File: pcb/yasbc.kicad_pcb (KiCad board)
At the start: 4 copper layers, 100 x 100 mm, 173 parts, among them J1 BOOT, J10 Conn_02x20_Odd_Even, J2 USB TTY, J3 AudioJack3, J4 1V5, J5 3V3, J6 1V2, J7 USB DEV, J8 Micro_SD_Card, J9 USB HOST, Q1 AO3401A, Q2 AO3401A, SW1 RESET, SW2 SW_SPDT, SW3 SW_SPDT, SW4 SW_SPDT, SW5 SW_SPDT, SW6 SW_5WAY, U1 BCT2028, U3 Allwinner_A13, U4 CH340E, U5 TD6810, U6 SE5120, U7 K4B4G1646E, U8 MPU-6050, Y1 24M

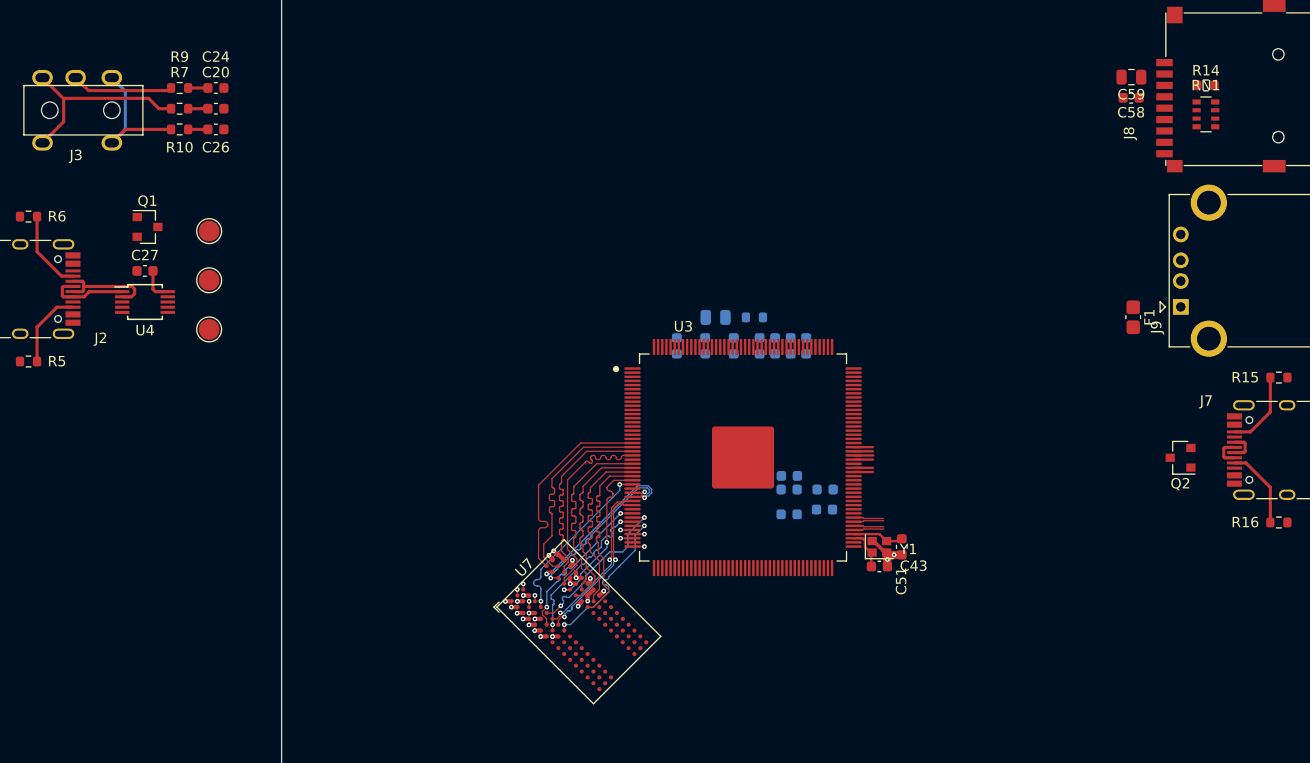
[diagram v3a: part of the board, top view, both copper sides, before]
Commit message: Routed DDR3 clock, address, command and control signals
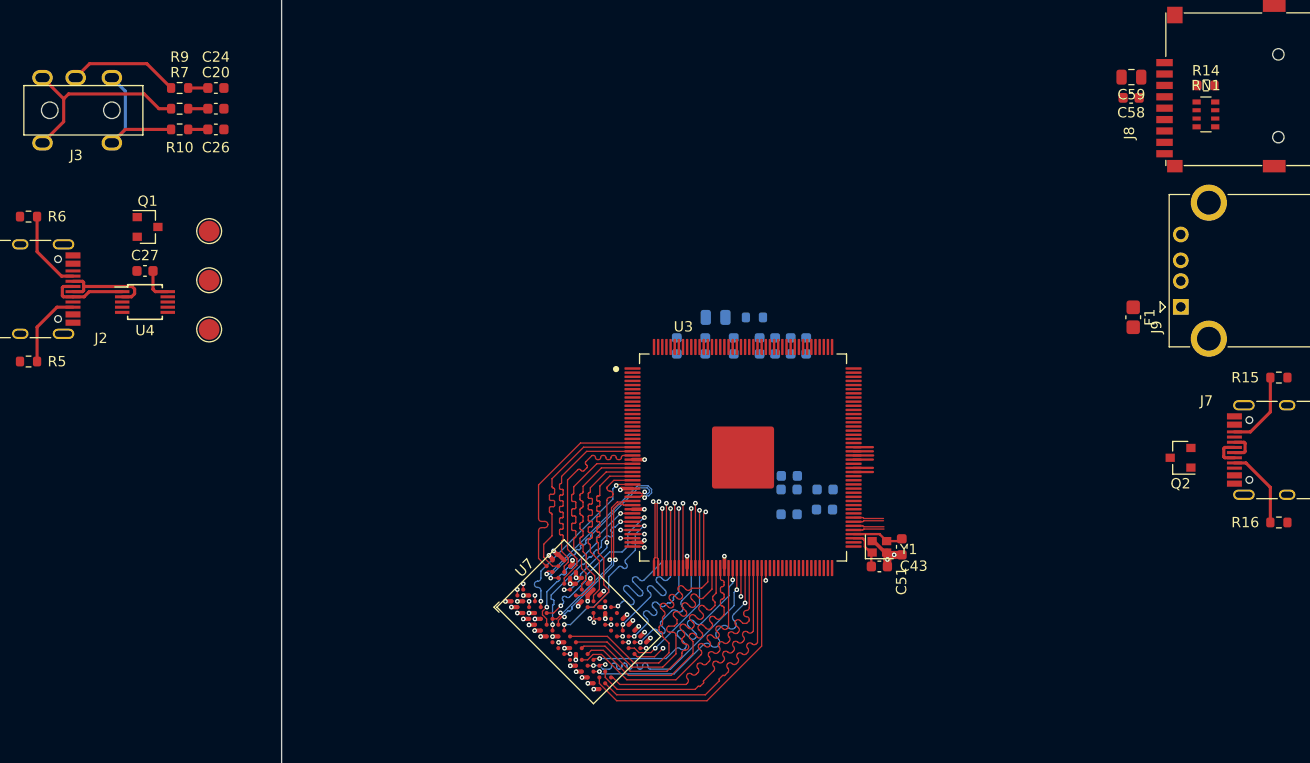
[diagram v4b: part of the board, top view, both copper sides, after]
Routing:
- net /DDR3_A7: track 0.00 -> 26.7 mm
- net /DDR3_RST: track 0.00 -> 26.5 mm
- net /DDR3_CAS: track 0.00 -> 26.5 mm
- net /DDR3_BA0: track 0.00 -> 26.5 mm
- net /DDR3_RAS: track 0.00 -> 26.5 mm
- net /DDR3_BA2: track 0.00 -> 26.5 mm
- net /DDR3_WE: track 0.00 -> 26.5 mm
- net /DDR3_A9: track 0.00 -> 26.5 mm
- net /DDR3_A13: track 0.00 -> 26.4 mm
- net /DDR3_ODT: track 0.00 -> 23.6 mm, vias 0 -> 2
- net /DDR3_A14: track 0.00 -> 23.6 mm, vias 0 -> 2
- net /DDR3_A11: track 0.00 -> 23.6 mm, vias 0 -> 2
- net /DDR3_A1: track 0.00 -> 23.6 mm, vias 0 -> 2
- net /DDR3_A8: track 0.00 -> 23.6 mm, vias 0 -> 2
- net /DDR3_A12: track 0.00 -> 23.6 mm, vias 0 -> 2
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
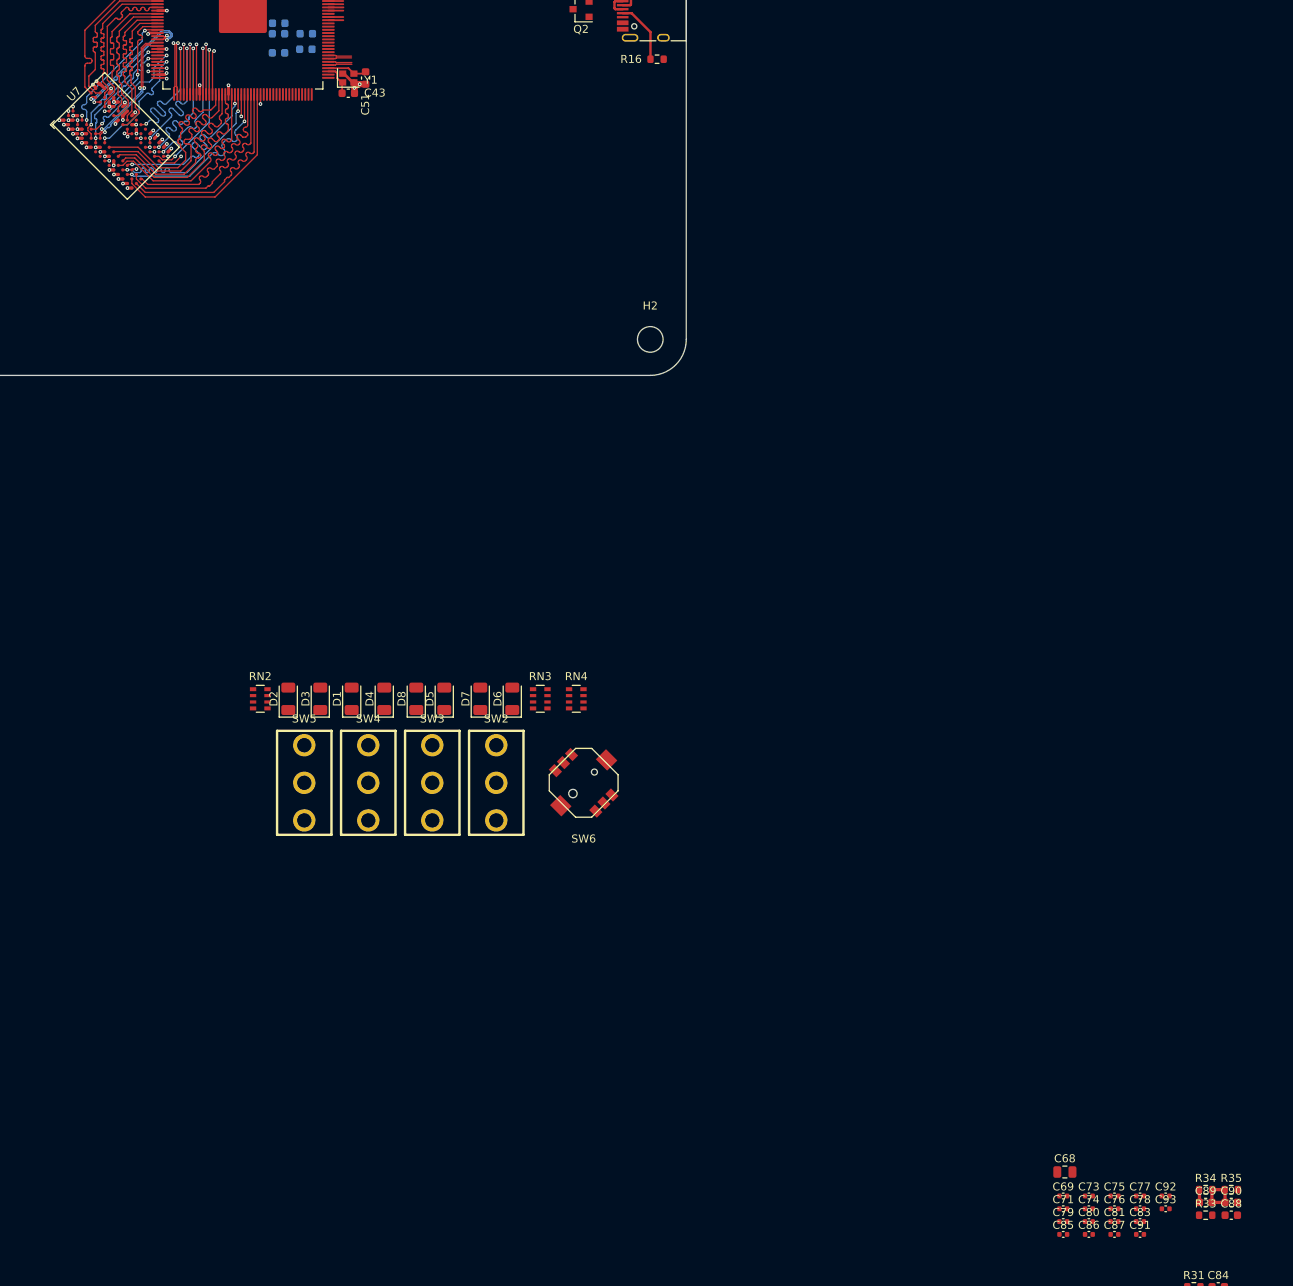
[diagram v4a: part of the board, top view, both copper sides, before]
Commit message: Worked on DDR3 decoupling caps
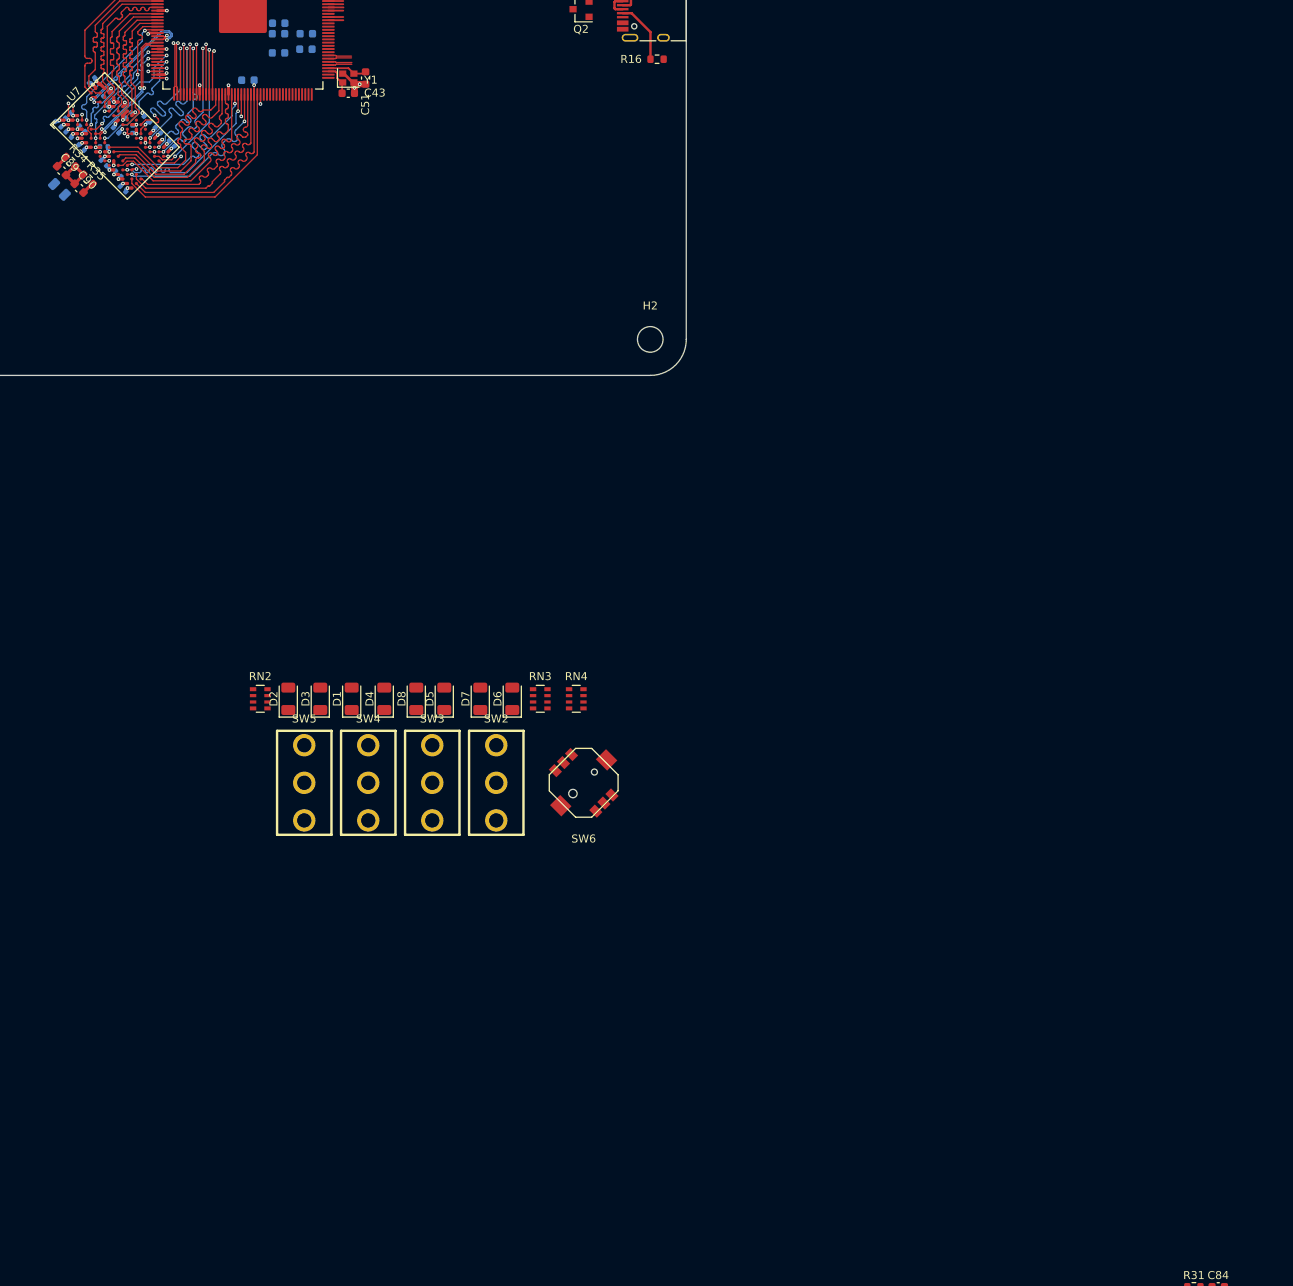
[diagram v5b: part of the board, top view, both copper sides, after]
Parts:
- removed C83: 0.1u, Capacitor_SMD:C_0402_1005Metric
- C68, C69, C71, C73, C74, C75, C76, C77, C78, C79, C80, C81, C85, C86, C87, C88, C91, C92, C93: moved to B.Cu
- R33: footprint Resistor_SMD:R_0603_1608Metric -> Resistor_SMD:R_0402_1005Metric; moved to B.Cu
- moved C89 192.6 mm to (58.9, -35.6), turned to -45 degrees
- moved C90 191.9 mm to (61.1, -33.4), turned to -45 degrees
- moved R34 191.4 mm to (60.0, -36.7), turned to -45 degrees
- moved R35 190.7 mm to (62.2, -34.5), turned to -45 degrees
- moved R33 190.5 mm to (69.6, -42.0), turned to 135 degrees
- moved C77 190.4 mm to (58.5, -41.4), turned to -45 degrees
- moved C81 190.3 mm to (59.8, -42.5), turned to 45 degrees
- moved C78 189.6 mm to (59.8, -40.1), turned to -45 degrees
- moved C93 188.1 mm to (65.7, -40.6), turned to -45 degrees
- moved C88 187.7 mm to (82.2, -46.9), turned to 180 degrees
- moved C76 186.5 mm to (65.1, -43.9), turned to -135 degrees
- moved C85 186.1 mm to (64.5, -45.2), turned to -135 degrees
- moved C71 186.1 mm to (62.7, -46.9), turned to 45 degrees
- moved C91 184.7 mm to (71.0, -40.6), turned to 135 degrees
- moved C87 184.1 mm to (64.2, -36.5), turned to -45 degrees
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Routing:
- net GND: track 34.8 -> 44.6 mm, vias 21 -> 23
- net +1V5: track 18.0 -> 27.7 mm
- net Net-(C89-Pad2): track 6.44 -> 13.4 mm, vias 0 -> 2
- net Net-(R33-Pad1): track 0.00 -> 2.07 mm, vias 0 -> 1
- net /DDR3_RST: track 26.5 -> 28.3 mm, vias 0 -> 1
- added copper zone on In1.Cu, net GND

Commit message: WIP
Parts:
- moved C86 2.66 mm to (65.7, -40.8), turned to -45 degrees
- moved C93 2.61 mm to (63.7, -38.9), turned to 0 degrees
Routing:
- net Net-(C89-Pad2): track 13.4 -> 16.5 mm
- net +1V5: track 27.7 -> 25.6 mm, vias 22 -> 24
- net GND: track 44.6 -> 44.1 mm, vias 23 -> 25
- added copper zone on In2.Cu, net +1V5

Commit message: PMIC PCB layout
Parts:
- removed J2: USB TTY, Connector_USB:USB_C_Receptacle_HRO_TYPE-C-31-M-12
- removed RN3: 1K, Resistor_SMD:R_Array_Convex_4x0603
- removed RN4: 47K, Resistor_SMD:R_Array_Convex_4x0603
- removed U8: MPU-6050, Sensor_Motion:InvenSense_QFN-24_4x4mm_P0.5mm
- added C100: 100n, Capacitor_SMD:C_0603_1608Metric, F.Cu at (262.1, -104.6)
- added C101: 100n, Capacitor_SMD:C_0603_1608Metric, F.Cu at (237.9, -64.2)
- added C102: 22p, Capacitor_SMD:C_0603_1608Metric, F.Cu at (229.9, -59.5)
- added C103: 100n, Capacitor_SMD:C_0603_1608Metric, F.Cu at (217.2, -57.1)
- added C104: 100n, Capacitor_SMD:C_0603_1608Metric, F.Cu at (274.1, -102.1)
- added C105: 22p, Capacitor_SMD:C_0603_1608Metric, F.Cu at (226.3, -69.5)
- added C106: 100n, Capacitor_SMD:C_0603_1608Metric, F.Cu at (244.4, -89.1)
- added C107: 100n, Capacitor_SMD:C_0603_1608Metric, F.Cu at (225.9, -57.0)
- added C45: 100n, Capacitor_SMD:C_0603_1608Metric, F.Cu at (217.9, -64.6)
- added C53: 100n, Capacitor_SMD:C_0603_1608Metric, F.Cu at (233.9, -62.0)
- added C6: 100n, Capacitor_SMD:C_0603_1608Metric, F.Cu at (84.1, -98.3)
- added C83: 100n, Capacitor_SMD:C_0603_1608Metric, F.Cu at (234.3, -72.0)
- added C94: 100n, Capacitor_SMD:C_0603_1608Metric, F.Cu at (257.7, -94.6)
- added C95: 100n, Capacitor_SMD:C_0603_1608Metric, F.Cu at (237.9, -66.7)
- added C96: 100n, Capacitor_SMD:C_0603_1608Metric, F.Cu at (217.0, -47.0)
- added C97: 100n, Capacitor_SMD:C_0603_1608Metric, F.Cu at (261.7, -97.1)
- added C98: 100n, Capacitor_SMD:C_0603_1608Metric, F.Cu at (209.0, -49.2)
- added C99: 100n, Capacitor_SMD:C_0603_1608Metric, F.Cu at (254.2, -85.1)
- added J11: Conn_02x20_Odd_Even, Connector_PinHeader_2.54mm:PinHeader_2x20_P2.54mm_Vertical, F.Cu at (168.9, -103.6)
- added L2: 2.2u, yasbc:Inductor_5.2x5.8x4.5mm, F.Cu at (93.9, -92.9)
- added R36: 5.1K, Resistor_SMD:R_0603_1608Metric, F.Cu at (213.4, -67.1)
- added R37: 5.1K, Resistor_SMD:R_0603_1608Metric, F.Cu at (218.3, -71.5)
- added R38: 10K, Resistor_SMD:R_0603_1608Metric, F.Cu at (193.0, -47.2)
- added R39: 100, Resistor_SMD:R_0603_1608Metric, F.Cu at (242.2, -76.9)
- added R40: 100, Resistor_SMD:R_0603_1608Metric, F.Cu at (274.1, -104.6)
- added R41: 22, Resistor_SMD:R_0603_1608Metric, F.Cu at (240.4, -89.4)
- added R42: 2K, Resistor_SMD:R_0603_1608Metric, F.Cu at (254.2, -80.1)
- added R43: 2K, Resistor_SMD:R_0603_1608Metric, F.Cu at (190.0, -74.6)
- added R44: 22, Resistor_SMD:R_0603_1608Metric, F.Cu at (209.8, -59.6)
- added R45: 10K, Resistor_SMD:R_0603_1608Metric, F.Cu at (222.3, -72.9)
- added R46: 22, Resistor_SMD:R_0603_1608Metric, F.Cu at (205.2, -54.2)
- added R47: 10K, Resistor_SMD:R_0603_1608Metric, F.Cu at (209.8, -62.1)
- added R48: 5.1K, Resistor_SMD:R_0603_1608Metric, F.Cu at (225.4, -76.7)
- added R49: 5.1K, Resistor_SMD:R_0603_1608Metric, F.Cu at (226.1, -80.0)
- added R50: 240 1%, Resistor_SMD:R_0603_1608Metric, F.Cu at (194.0, -74.6)
- added R51: 5.1K, Resistor_SMD:R_0603_1608Metric, F.Cu at (253.6, -95.2)
- added R52: 5.1K, Resistor_SMD:R_0603_1608Metric, F.Cu at (246.2, -83.6)
- C1, C25: value 1u -> 100n
- C10, C12: value 0.1u -> 6.8p; moved to F.Cu
- C11, C13: value 0.1u -> 33p; moved to F.Cu
- C14, C8: value 10u -> 100n; moved to F.Cu
- C15, C16, C17, C21, C3, C33, C37, C38, C4, C41, C42, C46, C47, C49, C50, C60, C7, C88, C9: value 0.1u -> 100n; moved to F.Cu
- C18, C19, C20, C24, C26, C27, C39, C58, C70, C72, C82, C90: value 0.1u -> 100n
- C2, C54, C55, C68: value 47u -> 100n; footprint Capacitor_SMD:C_0805_2012Metric -> Capacitor_SMD:C_0603_1608Metric; moved to F.Cu
- C22, C23, C28, C34, C36: value 0.1u -> 10u; moved to F.Cu
- C30, C35, C57: moved to F.Cu
- C31, C62, C89: value 0.1u -> 10u
- C32: value DNF -> 10u
- C40: value 10u -> 47u; moved to F.Cu
- C43, C51: value 22p -> 100n
- C48, C63, C64, C65, C66, C67: value 10u -> 100n
- C5: value DNF -> 100n
- C52: value 1u -> 100n; moved to F.Cu
- C56: value 0.1u -> 47u; moved to F.Cu
- C59: value 47u -> 100n; footprint Capacitor_SMD:C_0805_2012Metric -> Capacitor_SMD:C_0603_1608Metric
- C61: value 0.1u -> 1u; moved to F.Cu
- C69: value 0.1u -> 10u; footprint Capacitor_SMD:C_0402_1005Metric -> Capacitor_SMD:C_0603_1608Metric; moved to F.Cu
- C71, C75, C76, C77, C78, C79, C80, C81, C85, C86, C91, C92, C93: value 0.1u -> 100n; footprint Capacitor_SMD:C_0402_1005Metric -> Capacitor_SMD:C_0603_1608Metric; moved to F.Cu
- C73, C74, C87: value 0.1u -> 47u; footprint Capacitor_SMD:C_0402_1005Metric -> Capacitor_SMD:C_0603_1608Metric; moved to F.Cu
- C84: value 0.1u 50V -> 100n 50V
- D1: value LED_Small -> 5V; footprint LED_SMD:LED_1206_3216Metric -> Diode_SMD:D_SMB
- D9: value 5V -> LED_Small; footprint Diode_SMD:D_SMB -> LED_SMD:LED_1206_3216Metric
- F1: footprint Fuse:Fuse_0805_2012Metric_Castellated -> Fuse:Fuse_0805_2012Metric_Pad1.15x1.40mm_HandSolder
- J1: value BOOT -> USB TTY; footprint Connector_PinHeader_2.54mm:PinHeader_1x02_P2.54mm_Vertical -> Connector_USB:USB_C_Receptacle_HRO_TYPE-C-31-M-12
- J10: value Conn_02x20_Odd_Even -> AudioJack3; footprint Connector_PinHeader_2.54mm:PinHeader_2x20_P2.54mm_Vertical -> yasbc:AudioJack
- J3: value AudioJack3 -> USB DEV; footprint yasbc:AudioJack -> Connector_USB:USB_C_Receptacle_HRO_TYPE-C-31-M-12
- J5: value 3V3 -> 1V5
- J6: value 1V2 -> USB HOST; footprint Connector_PinHeader_2.54mm:PinHeader_1x02_P2.54mm_Vertical -> Connector_USB:USB_A_CONNFLY_DS1095-WNR0
- J7: value USB DEV -> 1V5; footprint Connector_USB:USB_C_Receptacle_HRO_TYPE-C-31-M-12 -> Connector_PinHeader_2.54mm:PinHeader_1x02_P2.54mm_Vertical
- J8: value Micro_SD_Card -> 1V5; footprint yasbc:microSD -> Connector_PinHeader_2.54mm:PinHeader_1x02_P2.54mm_Vertical
- J9: value USB HOST -> BOOT; footprint Connector_USB:USB_A_CONNFLY_DS1095-WNR0 -> Connector_PinHeader_2.54mm:PinHeader_1x02_P2.54mm_Vertical
- L1: value 4.7u -> 2.2u; footprint Inductor_SMD:L_1008_2520Metric -> yasbc:Inductor_5.2x5.8x4.5mm
- R1, R12, R2, R20, R21, R22: value 10K -> 5.1K
- R10: value 22 -> 402K
- R11: value 10K -> 200K; moved to F.Cu
- R13: value 200K -> 5.1K; moved to F.Cu
- R15, R24, R25, R26, R31, R32: value 5.1K -> 47K
- R16: value 5.1K -> 10K
- R17: value 240 1% -> 10K; moved to F.Cu
- R18, R19: value 2K -> 10K; moved to F.Cu
- R27: value 10K -> 2K
- R28: value 100 -> 2K
- R29: value 100 -> 240 1%
- R3: value 5.1K -> 887
- R33: value 240 1% -> 47K; footprint Resistor_SMD:R_0402_1005Metric -> Resistor_SMD:R_0603_1608Metric; moved to F.Cu
- R34: value 2K -> 200K
- R35: value 2K -> 47K
- R4: value 5.1K -> 280K
- R5: value 5.1K -> 200K
- R6: value 5.1K -> 562K
- R7: value 22 -> 100K
- R8: value 10K -> 604K
- R9: value 22 -> 232K
- RN1: value 47K -> 1K
- SW1: value RESET -> SW_SPDT; footprint yasbc:HYP-1TS002B-2500-4300-CT -> yasbc:SS-12D10
- SW5: value SW_SPDT -> SW_5WAY; footprint yasbc:SS-12D10 -> yasbc:Switches_ALPS-SKRHAAE010
- SW6: value SW_5WAY -> RESET; footprint yasbc:Switches_ALPS-SKRHAAE010 -> yasbc:HYP-1TS002B-2500-4300-CT
- U1: value BCT2028 -> LM26480; footprint Package_TO_SOT_SMD:SOT-23-5 -> Package_DFN_QFN:WQFN-24-1EP_4x4mm_P0.5mm_EP2.6x2.6mm
- U3: value Allwinner_A13 -> CH340E; footprint yasbc:LQFP-176_20x20mm_P0.4mm_PAD -> Package_SO:MSOP-10_3x3mm_P0.5mm
- U4: value CH340E -> Allwinner_A13; footprint Package_SO:MSOP-10_3x3mm_P0.5mm -> yasbc:LQFP-176_20x20mm_P0.4mm_PAD
- U5: value TD6810 -> uSD_Card; footprint Package_TO_SOT_SMD:TSOT-23-5 -> yasbc:microSD
- U6: value SE5120 -> MPU-6050; footprint Package_TO_SOT_SMD:SOT-223-3_TabPin2 -> Sensor_Motion:InvenSense_QFN-24_4x4mm_P0.5mm
- moved C61 331.1 mm to (258.2, -87.1), turned to 0 degrees
- moved C60 330.1 mm to (257.7, -97.1), turned to 0 degrees
- moved C15 326.2 mm to (261.7, -99.6)
- moved J6 323.6 mm to (57.4, -96.4), turned to 180 degrees
- moved C29 317.8 mm to (82.1, -100.1)
- moved C54 316.9 mm to (265.7, -94.6), turned to 0 degrees
- moved C37 310.7 mm to (248.4, -88.6)
- moved C41 309.4 mm to (246.3, -73.5)
- moved L1 308.8 mm to (79.5, -92.9), turned to -90 degrees
- moved C35 307.9 mm to (250.3, -76.0), turned to 0 degrees
- moved C33 305.5 mm to (242.2, -79.4)
- moved R18 303.2 mm to (226.3, -72.0), turned to 0 degrees
- moved R13 301.4 mm to (242.3, -71.8), turned to 0 degrees
- moved C5 300.6 mm to (89.1, -98.2)
- moved C1 296.7 mm to (83.1, -95.9), turned to 90 degrees
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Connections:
- C1 pad 1: VBUS -> GND
- C1 pad 2: GND -> +5V
- C10 pad 1: +3V3 -> +1V2
- C10 pad 2: GND -> /P_FB1
- C11 pad 1: +1V2 -> /P_FB1
- C12 pad 2: GND -> /P_FB2
- C13 pad 1: +1V2 -> /P_FB2
- C14 pad 1: +3V3 -> +1V8
- C15 pad 1: +3V3 -> +1V8
- C16 pad 1: +1V2 -> +1V8
- C17 pad 1: +3V3 -> +1V8
- C18 pad 1: /RESET -> +1V2
- C19 pad 1: Net-(C19-Pad1) -> +3V3
- C2 pad 1: +1V2 -> +5V
- C20 pad 1: Net-(C20-Pad1) -> +1V8
- C21 pad 1: +3V3 -> +1V8
- C24 pad 1: Net-(C24-Pad1) -> +1V8
- C25 pad 1: Net-(C25-Pad1) -> +3V3
- C26 pad 1: Net-(C26-Pad1) -> +1V8
- C27 pad 1: +3V3 -> +1V5
- C28 pad 1: Net-(C28-Pad1) -> +1V8
- C29 pad 1: VBUS -> +1V5
- C3 pad 1: +1V2 -> +5V
- C30 pad 1: Net-(C28-Pad1) -> /SW_DOWN
- C31 pad 1: VBUS -> /SW_UP
- C32 pad 1: Net-(C32-Pad1) -> /SW_RIGHT
- C33 pad 1: +1V5 -> /SW_R2R
- C34 pad 1: +1V2 -> /SW_CENTER
- C35 pad 1: GND -> /SW_LEFT
- C35 pad 2: +3V3 -> GND
- C36 pad 1: Net-(C36-Pad1) -> +3V3
- C37 pad 1: +1V5 -> +1V2
- C38 pad 1: +1V2 -> +3V3
- C39 pad 1: Net-(C39-Pad1) -> +1V2
- C4 pad 1: +1V2 -> +5V
- C40 pad 1: Net-(C36-Pad1) -> +1V2
- C41 pad 1: +1V5 -> +3V3
- C43 pad 1: Net-(C43-Pad1) -> +1V2
- C44 pad 1: Net-(C44-Pad1) -> +3V3
- C46 pad 1: +1V5 -> +1V2
- C48 pad 1: Net-(C39-Pad1) -> +3V3
- C49 pad 1: +1V5 -> +3V3
- C5 pad 1: Net-(C5-Pad1) -> +3V3
- C51 pad 1: Net-(C51-Pad1) -> +1V2
- C52 pad 1: Net-(C52-Pad1) -> +3V3
- C54 pad 1: +1V5 -> /A13_SVREF
- C55 pad 1: +1V2 -> +3V3
- C56 pad 1: Net-(C56-Pad1) -> +3V3
- C57 pad 1: Net-(C56-Pad1) -> +3V3
- C58 pad 1: +3V3 -> Net-(C58-Pad1)
- C59 pad 1: +3V3 -> +1V5
- C60 pad 1: +1V5 -> +1V2
- C60 pad 2: Net-(C60-Pad2) -> GND
- C61 pad 1: Net-(C60-Pad2) -> Net-(C61-Pad1)
- C62 pad 1: /SW_R2R -> Net-(C58-Pad1)
- C63 pad 1: /SW_DOWN -> +1V5
- C64 pad 1: /SW_UP -> +1V2
- C65 pad 1: /SW_RIGHT -> +1V5
- C66 pad 1: /SW_CENTER -> +1V2
- C67 pad 1: /SW_LEFT -> +1V5
- C68 pad 1: +1V5 -> +1V2
- C69 pad 1: +1V5 -> Net-(C69-Pad1)
- C7 pad 1: +1V2 -> GND
- C7 pad 2: GND -> +3V3
- C70 pad 1: +3V3 -> Net-(C69-Pad1)
- C72 pad 1: +3V3 -> +1V2
- C74 pad 1: +1V5 -> +1V2
- C75 pad 1: +1V5 -> Net-(C75-Pad1)
- C76 pad 1: +1V5 -> /RESET
- C77 pad 1: +1V5 -> /DDR3_RST
- C78 pad 1: +1V5 -> Net-(C78-Pad1)
- C79 pad 2: GND -> /DDR3_REF
- C8 pad 1: +3V3 -> +1V8
- C80 pad 1: +1V5 -> /DDR3_REF
- C81 pad 1: +1V5 -> Net-(C81-Pad1)
- C85 pad 1: +1V5 -> Net-(C85-Pad1)
- C86 pad 1: +1V5 -> +3V3
- C88 pad 1: /DDR3_RST -> +1V5
- C89 pad 1: +1V5 -> Net-(C85-Pad1)
- C89 pad 2: Net-(C89-Pad2) -> GND
- C9 pad 1: +1V2 -> +1V8
- C90 pad 1: Net-(C89-Pad2) -> +1V5
- D1 pad 1: GND -> +5V
- D1 pad 2: Net-(D1-Pad2) -> GND
- D9 pad 1: VBUS -> GND
- D9 pad 2: GND -> Net-(D9-Pad2)
- F1 pad 2: VBUS -> +5V
- J4 pad 1: +1V5 -> +1V2
- J4 pad 2: Net-(C25-Pad1) -> GND
- J5 pad 2: Net-(C39-Pad1) -> GND
- J6 pad 1: +1V2 -> Net-(F1-Pad1)
- J6 pad 2: Net-(C44-Pad1) -> /USB_HOST_D-
- J8 pad 1: /SD_D2 -> +1V5
- J8 pad 2: /SD_D3 -> GND
- J9 pad 1: Net-(F1-Pad1) -> GND
- J9 pad 2: /USB_HOST_D- -> /BOOT
- L1 pad 1: Net-(L1-Pad1) -> /P_SW1
- L1 pad 2: Net-(C44-Pad1) -> +1V2
- Q1 pad 2: VBUS -> +5V
- Q1 pad 3: Net-(J2-PadA4) -> Net-(J1-PadA4)
- Q2 pad 2: VBUS -> +5V
- Q2 pad 3: Net-(J7-PadA4) -> Net-(J3-PadA4)
- R1 pad 1: Net-(C5-Pad1) -> Net-(J1-PadA5)
- R1 pad 2: VBUS -> GND
- R10 pad 1: Net-(C26-Pad1) -> +1V5
- R10 pad 2: Net-(J3-PadT) -> /P_FBL2
- R11 pad 1: +3V3 -> /P_FBL2
- R11 pad 2: Net-(R11-Pad2) -> GND
- R12 pad 1: Net-(C32-Pad1) -> Net-(J3-PadA5)
- R12 pad 2: VBUS -> GND
- R13 pad 1: Net-(C36-Pad1) -> Net-(J3-PadB5)
- R14 pad 1: +3V3 -> /SW_DOWN
- R14 pad 2: /SD_D1 -> GND
- R15 pad 1: Net-(J7-PadB5) -> /SW_UP
- R16 pad 1: Net-(J7-PadA5) -> /SW_R2R
- R16 pad 2: GND -> Net-(R16-Pad2)
- R17 pad 2: GND -> Net-(R17-Pad2)
- R18 pad 1: +1V5 -> Net-(R18-Pad1)
- R18 pad 2: Net-(C60-Pad2) -> Net-(R18-Pad2)
- R19 pad 1: Net-(C60-Pad2) -> Net-(R19-Pad1)
- R19 pad 2: GND -> Net-(R19-Pad2)
- R2 pad 1: +3V3 -> Net-(J1-PadB5)
- R2 pad 2: /BOOT -> GND
- R20 pad 1: /SW_R2R -> Net-(R17-Pad1)
- R20 pad 2: Net-(R20-Pad2) -> /SW_R2R
- R21 pad 1: Net-(R21-Pad1) -> Net-(R18-Pad1)
- R21 pad 2: Net-(R21-Pad2) -> Net-(R17-Pad1)
- R22 pad 1: Net-(R22-Pad1) -> Net-(R19-Pad1)
- R22 pad 2: Net-(R22-Pad2) -> Net-(R18-Pad1)
- R23 pad 1: Net-(R23-Pad1) -> GND
- R23 pad 2: Net-(R23-Pad2) -> Net-(R19-Pad1)
- R24 pad 1: Net-(R21-Pad1) -> /SW_RIGHT
- R24 pad 2: /SW_R2R -> GND
- R25 pad 1: Net-(R22-Pad1) -> /SW_CENTER
- R25 pad 2: Net-(R21-Pad1) -> GND
- R26 pad 1: Net-(R23-Pad1) -> /SW_LEFT
- R26 pad 2: Net-(R22-Pad1) -> GND
- R27 pad 1: GND -> +1V5
- R27 pad 2: Net-(R23-Pad1) -> /A13_SVREF
- R28 pad 1: Net-(R28-Pad1) -> /A13_SVREF
- R28 pad 2: /TTY_TX -> GND
- R29 pad 2: /TTY_RX -> GND
- R3 pad 1: +3V3 -> GND
- R3 pad 2: /I2C_SCL -> Net-(R3-Pad2)
- R30 pad 1: /SW_LEFT -> +3V3
- R30 pad 2: GND -> /SD_CMD
- R31 pad 2: /MPU_SCL -> /SD_D3
- R32 pad 2: /MPU_SDA -> /SD_D2
- R33 pad 1: Net-(R33-Pad1) -> +3V3
- R33 pad 2: GND -> /SD_D1
- R34 pad 1: +1V5 -> Net-(C58-Pad1)
- R34 pad 2: Net-(C89-Pad2) -> GND
- R35 pad 1: Net-(C89-Pad2) -> +3V3
- R35 pad 2: GND -> /SD_D0
- R4 pad 1: +3V3 -> +1V2
- R4 pad 2: /I2C_SDA -> /P_FB1
- R5 pad 1: Net-(J2-PadB5) -> /P_FB1
- R6 pad 1: Net-(J2-PadA5) -> +3V3
- R6 pad 2: GND -> /P_FB2
- R7 pad 1: Net-(C20-Pad1) -> /P_FB2
- R7 pad 2: Net-(J3-PadS) -> GND
- R8 pad 1: +3V3 -> +1V8
- R8 pad 2: /RESET -> /P_FBL1
- R9 pad 1: Net-(C24-Pad1) -> /P_FBL1
- R9 pad 2: Net-(J3-PadR) -> GND
- RN1 pad 1: /SD_D2 -> /LED3
- RN1 pad 2: /SD_D3 -> /LED1
- RN1 pad 3: /SD_CMD -> /LED2
- RN1 pad 4: /SD_D0 -> /LED4
- RN1 pad 5: +3V3 -> Net-(D5-Pad2)
- RN1 pad 6: +3V3 -> Net-(D4-Pad2)
- RN1 pad 7: +3V3 -> Net-(D3-Pad2)
- RN1 pad 8: +3V3 -> Net-(D2-Pad2)
- RN2 pad 1: /LED3 -> Net-(D6-Pad2)
- RN2 pad 2: /LED1 -> Net-(D7-Pad2)
- RN2 pad 3: /LED2 -> Net-(D8-Pad2)
- RN2 pad 4: /LED4 -> Net-(D9-Pad2)
- RN2 pad 5: Net-(D4-Pad2) -> /LED5
- RN2 pad 6: Net-(D3-Pad2) -> /LED7
- RN2 pad 7: Net-(D2-Pad2) -> /LED8
- RN2 pad 8: Net-(D1-Pad2) -> /LED6
- SW1 pad 1: GND -> +3V3
- SW1 pad 2: /RESET -> Net-(R16-Pad2)
- SW2 pad 2: Net-(R20-Pad2) -> Net-(R17-Pad2)
- SW3 pad 2: Net-(R21-Pad2) -> Net-(R18-Pad2)
- SW4 pad 2: Net-(R22-Pad2) -> Net-(R19-Pad2)
- SW5 pad 1: +3V3 -> /SW_UP
- SW5 pad 2: Net-(R23-Pad2) -> /SW_CENTER
- SW5 pad 3: GND -> /SW_LEFT
- SW6 pad 1: /SW_UP -> GND
- SW6 pad 2: /SW_CENTER -> /RESET
- U1 pad 1: VBUS -> +5V
- U1 pad 3: Net-(C5-Pad1) -> unconnected-(U1-Pad3)
- U1 pad 4: Net-(C19-Pad1) -> GND
- U1 pad 5: Net-(C25-Pad1) -> /P_SW1
- U3 pad 1: unconnected-(U3-Pad1) -> Net-(J1-PadA6)
- U3 pad 10: /SPI2_CS1 -> +3V3
- U3 pad 2: unconnected-(U3-Pad2) -> Net-(J1-PadA7)
- U3 pad 3: unconnected-(U3-Pad3) -> GND
- U3 pad 4: +1V2 -> unconnected-(U3-Pad4)
- U3 pad 5: +3V3 -> unconnected-(U3-Pad5)
- U3 pad 7: unconnected-(U3-Pad7) -> +3V3
- U3 pad 8: unconnected-(U3-Pad8) -> /TTY_RX
- U3 pad 9: +1V2 -> /TTY_TX
- U4 pad 1: Net-(J2-PadA6) -> unconnected-(U4-Pad1)
- U4 pad 10: +3V3 -> /SPI2_CS1
- U4 pad 2: Net-(J2-PadA7) -> unconnected-(U4-Pad2)
- U4 pad 3: GND -> /SW_RIGHT
- U4 pad 4: unconnected-(U4-Pad4) -> +1V2
- U4 pad 5: unconnected-(U4-Pad5) -> +3V3
- U4 pad 6: unconnected-(U4-Pad6) -> /SW_LEFT
- U4 pad 7: +3V3 -> /SW_DOWN
- U4 pad 8: /TTY_RX -> /SW_UP
- U4 pad 9: /TTY_TX -> +1V2
- U5 pad 1: Net-(C32-Pad1) -> /SD_D2
- U5 pad 2: GND -> /SD_D3
- U5 pad 3: Net-(L1-Pad1) -> /SD_CMD
- U5 pad 4: VBUS -> +3V3
- U5 pad 5: Net-(C44-Pad1) -> /SD_CLK
- U6 pad 2: Net-(C39-Pad1) -> unconnected-(U6-Pad2)
- U6 pad 3: VBUS -> unconnected-(U6-Pad3)
- U7 pad H1: Net-(C89-Pad2) -> /DDR3_REF
- U7 pad L8: Net-(R33-Pad1) -> Net-(R50-Pad1)
- U7 pad M8: Net-(C89-Pad2) -> /DDR3_REF
- Y1 pad 1: Net-(C43-Pad1) -> Net-(C102-Pad1)
- Y1 pad 3: Net-(C51-Pad1) -> Net-(C105-Pad1)
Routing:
- net GND: track 44.1 -> 1.92 mm, vias 25 -> 52
- net +3V3: track 3.29 -> 32.5 mm, vias 0 -> 8
- net /DDR3_RST: track 28.3 -> 0.00 mm, vias 1 -> 0
- net /DDR3_A7: track 26.7 -> 0.00 mm
- net /DDR3_CAS: track 26.5 -> 0.00 mm
- net /DDR3_BA0: track 26.5 -> 0.00 mm
- net /DDR3_RAS: track 26.5 -> 0.00 mm
- net /DDR3_BA2: track 26.5 -> 0.00 mm
- net /DDR3_WE: track 26.5 -> 0.00 mm
- net /DDR3_A9: track 26.5 -> 0.00 mm
- net /DDR3_A13: track 26.4 -> 0.00 mm
- net /DDR3_ODT: track 23.6 -> 0.00 mm, vias 2 -> 0
- net /DDR3_A14: track 23.6 -> 0.00 mm, vias 2 -> 0
- net /DDR3_A11: track 23.6 -> 0.00 mm, vias 2 -> 0
- net /DDR3_A1: track 23.6 -> 0.00 mm, vias 2 -> 0
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- added copper zone on F.Cu, net +1V2
- added copper zone on B.Cu, net +3V3
- added copper zone on F.Cu, net +3V3
- added copper zone on B.Cu, net +5V
- added copper zone on F.Cu, net +5V
- added copper zone on F.Cu, net /P_FB1
- added copper zone on F.Cu, net /P_FB2
- added copper zone on F.Cu, net GND
- removed copper zone on In2.Cu, net +1V5
